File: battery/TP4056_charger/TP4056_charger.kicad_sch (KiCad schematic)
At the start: 19 parts

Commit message: separate charger and battery
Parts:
- removed BAT_J1: BATT, ErgoCai.pretty:JST_PH_S2B-PH-K_1x02_P2.00mm_Horizontal, symbol Connector_Generic:Conn_01x02

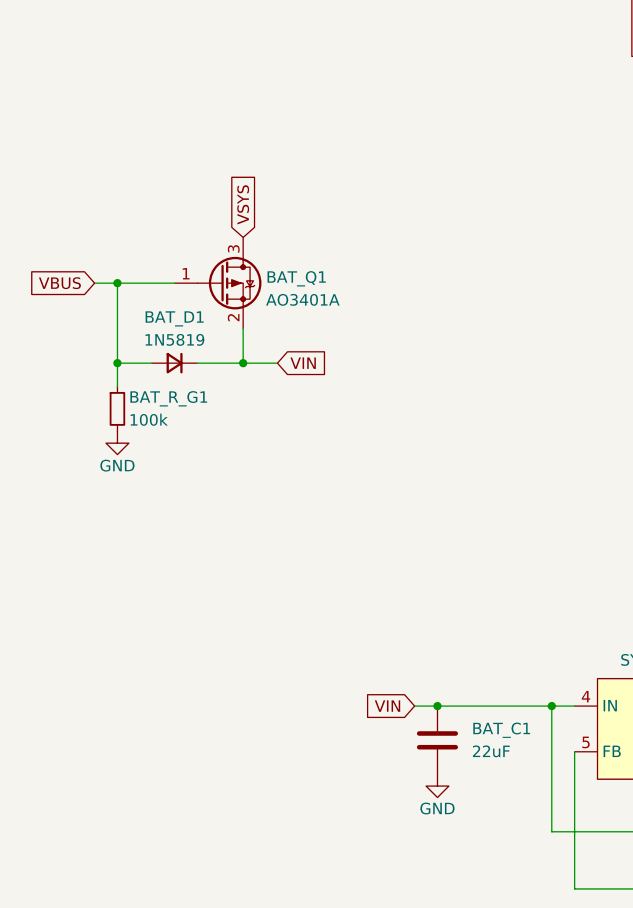
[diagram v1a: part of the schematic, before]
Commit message: remove vin in charger
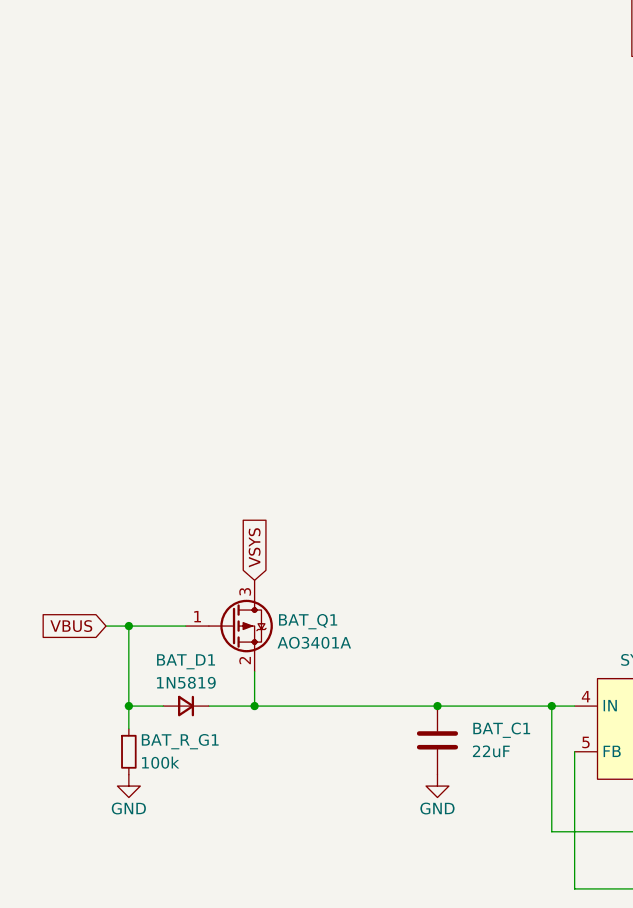
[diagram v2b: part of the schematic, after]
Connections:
- net VIN: no longer names the net of BAT_C1.1, BAT_D1.1 (K), BAT_Q1.2 (S), BAT_U1.1 (EN), BAT_U1.4 (IN)
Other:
- moved on the sheet: BAT_D1, BAT_Q1, BAT_R_G1
